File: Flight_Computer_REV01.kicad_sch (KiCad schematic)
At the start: 21 parts, among them CON1 AVR-JTAG-10, J10 Conn_02x12_Odd_Even, J2 Conn_02x03_Counter_Clockwise, J3 Conn_02x03_Counter_Clockwise, J4 Conn_02x05_Top_Bottom, J5 Conn_02x16_Top_Bottom, J6 Conn_02x16_Top_Bottom, J7 Conn_02x10_Odd_Even, J8 Conn_02x16_Top_Bottom, J9 Conn_02x16_Top_Bottom

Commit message: updated layouts, added motor
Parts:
- removed J4: Conn_02x05_Top_Bottom, Connector_PinHeader_2.54mm:PinHeader_2x05_P2.54mm_Vertical, symbol Connector_Generic:Conn_02x05_Top_Bottom
- added J3: AMB POWER, Connector_PinHeader_2.54mm:PinHeader_2x04_P2.54mm_Vertical, symbol Connector_Generic:Conn_02x04_Counter_Clockwise
- added J4: INPUT POWER PASSTHROUGH, Connector_PinHeader_2.54mm:PinHeader_2x03_P2.54mm_Vertical, symbol Connector_Generic:Conn_02x03_Counter_Clockwise
- CON1: now not fitted
- J7: footprint Connector_PinSocket_2.54mm:PinSocket_2x10_P2.54mm_Vertical -> Connector_PinSocket_2.54mm:PinSocket_2x14_P2.54mm_Vertical; symbol Connector_Generic:Conn_02x10_Odd_Even -> Connector_Generic:Conn_02x14_Odd_Even
- J8: renamed from J10; value Conn_02x12_Odd_Even -> Conn_02x18_Odd_Even; footprint Connector_PinHeader_2.54mm:PinHeader_2x12_P2.54mm_Vertical -> Connector_PinSocket_1.27mm:PinSocket_2x26_P1.27mm_Vertical; symbol Connector_Generic:Conn_02x18_Odd_Even -> Connector_Generic:Conn_02x26_Odd_Even
- renumbered C3 to C1, C4 to C2, C5 to C3, C6 to C4, C7 to C5, C8 to C6, C9 to C7, J2 to J1, J9 to J10, J3 to J2, J8 to J9
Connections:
- net GND: now also J7.11 (Pin_11), J7.12 (Pin_12), J7.13 (Pin_13), J7.14 (Pin_14), J7.19 (Pin_19), J7.20 (Pin_20), J7.21 (Pin_21), J7.22 (Pin_22), J8.30 (Pin_30), J3.2 (Pin_2), J3.4 (Pin_4), J3.6 (Pin_6), J3.8 (Pin_8); no longer J7.10 (Pin_10), J7.15 (Pin_15), J7.16 (Pin_16), J7.17 (Pin_17), J7.18 (Pin_18), J7.5 (Pin_5), J7.7 (Pin_7), J7.8 (Pin_8), J8.24 (Pin_24), J8.36 (Pin_36)
- net MTR_SCLK: now also J8.34 (Pin_34); no longer J8.22 (Pin_22)
- net MTR_SDI: now also J8.20 (Pin_20); no longer J8.14 (Pin_14)
- net MTR_SDO: now also J8.9 (Pin_9); no longer J8.3 (Pin_3)
- net MTR_WHA_EN: now also J8.11 (Pin_11); no longer J8.5 (Pin_5)
- net MTR_WHA_HALLA: now also J8.36 (Pin_36); no longer J8.30 (Pin_30)
- net MTR_WHA_HALLB: now also J8.38 (Pin_38); no longer J8.32 (Pin_32)
- net MTR_WHA_HALLC: now also J8.40 (Pin_40); no longer J8.34 (Pin_34)
- net MTR_WHA_INA_H: now also J8.31 (Pin_31); no longer J8.19 (Pin_19)
- net MTR_WHA_INA_L: now also J8.12 (Pin_12); no longer J8.6 (Pin_6)
- net MTR_WHA_INB_H: now also J8.21 (Pin_21); no longer J8.15 (Pin_15)
- net MTR_WHA_INB_L: now also J8.23 (Pin_23); no longer J8.17 (Pin_17)
- net MTR_WHA_INC_H: now also J8.32 (Pin_32); no longer J8.20 (Pin_20)
- net MTR_WHA_INC_L: now also J8.24 (Pin_24); no longer J8.18 (Pin_18)
- net MTR_WHA_SCS: now also J8.7 (Pin_7); no longer J8.1 (Pin_1)
- net MTR_WHB_EN: now also J8.19 (Pin_19); no longer J8.13 (Pin_13)
- net MTR_WHB_HALLA: now also J8.35 (Pin_35); no longer J8.29 (Pin_29)
- net MTR_WHB_HALLB: now also J8.37 (Pin_37); no longer J8.31 (Pin_31)
- net MTR_WHB_HALLC: now also J8.39 (Pin_39); no longer J8.33 (Pin_33)
- net MTR_WHB_INA_H: now also J8.14 (Pin_14); no longer J8.8 (Pin_8)
- net MTR_WHB_INA_L: now also J8.16 (Pin_16); no longer J8.10 (Pin_10)
- net MTR_WHB_INB_H: now also J8.15 (Pin_15); no longer J8.9 (Pin_9)
- net MTR_WHB_INB_L: now also J8.17 (Pin_17); no longer J8.11 (Pin_11)
- net MTR_WHB_INC_H: now also J8.33 (Pin_33); no longer J8.21 (Pin_21)
- net MTR_WHB_INC_L: now also J8.13 (Pin_13); no longer J8.7 (Pin_7)
- net MTR_WHB_SCS: now also J8.18 (Pin_18); no longer J8.12 (Pin_12)
- net MTR_WHB_WAKE: now also J8.8 (Pin_8); no longer J8.2 (Pin_2)
- net N5V: now also J7.2 (Pin_2), J7.4 (Pin_4); no longer J7.20 (Pin_20)
- net P12V: now also J7.10 (Pin_10); no longer J7.6 (Pin_6)
- net P3V3: now also J8.29 (Pin_29); no longer J8.23 (Pin_23), J8.35 (Pin_35)
- net P4V5: now also J7.15 (Pin_15), J7.16 (Pin_16), J7.17 (Pin_17), J7.18 (Pin_18); no longer J7.11 (Pin_11), J7.12 (Pin_12), J7.13 (Pin_13), J7.14 (Pin_14)
- net P5V: now also J7.1 (Pin_1), J7.3 (Pin_3); no longer J7.19 (Pin_19)
- net VAMB: now also J3.1 (Pin_1), J3.3 (Pin_3), J3.5 (Pin_5), J3.7 (Pin_7); no longer J7.1 (Pin_1), J7.2 (Pin_2), J7.3 (Pin_3), J7.4 (Pin_4)
- net _MTR_WHA_nFAULT: now also J8.22 (Pin_22); no longer J8.16 (Pin_16)
- net _MTR_WHB_nFAULT: now also J8.10 (Pin_10); no longer J8.4 (Pin_4)
- new net: J7.5 (Pin_5), J7.7 (Pin_7)
- new net: J7.6 (Pin_6), J7.8 (Pin_8)
- new net 28_IN: J4.1 (Pin_1), J4.2 (Pin_2), J4.3 (Pin_3)
- new net 28_RET: J4.4 (Pin_4), J4.5 (Pin_5), J4.6 (Pin_6)
- new net MTR_WHA_VSNS_A: J8.42 (Pin_42)
- new net MTR_WHA_VSNS_B: J8.44 (Pin_44)
- new net MTR_WHA_VSNS_C: J8.46 (Pin_46)
- new net MTR_WHB_VSNS_A: J8.41 (Pin_41)
- new net MTR_WHB_VSNS_B: J8.43 (Pin_43)
- new net MTR_WHB_VSNS_C: J8.45 (Pin_45)
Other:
- added sheet Motor (Motor.kicad_sch)

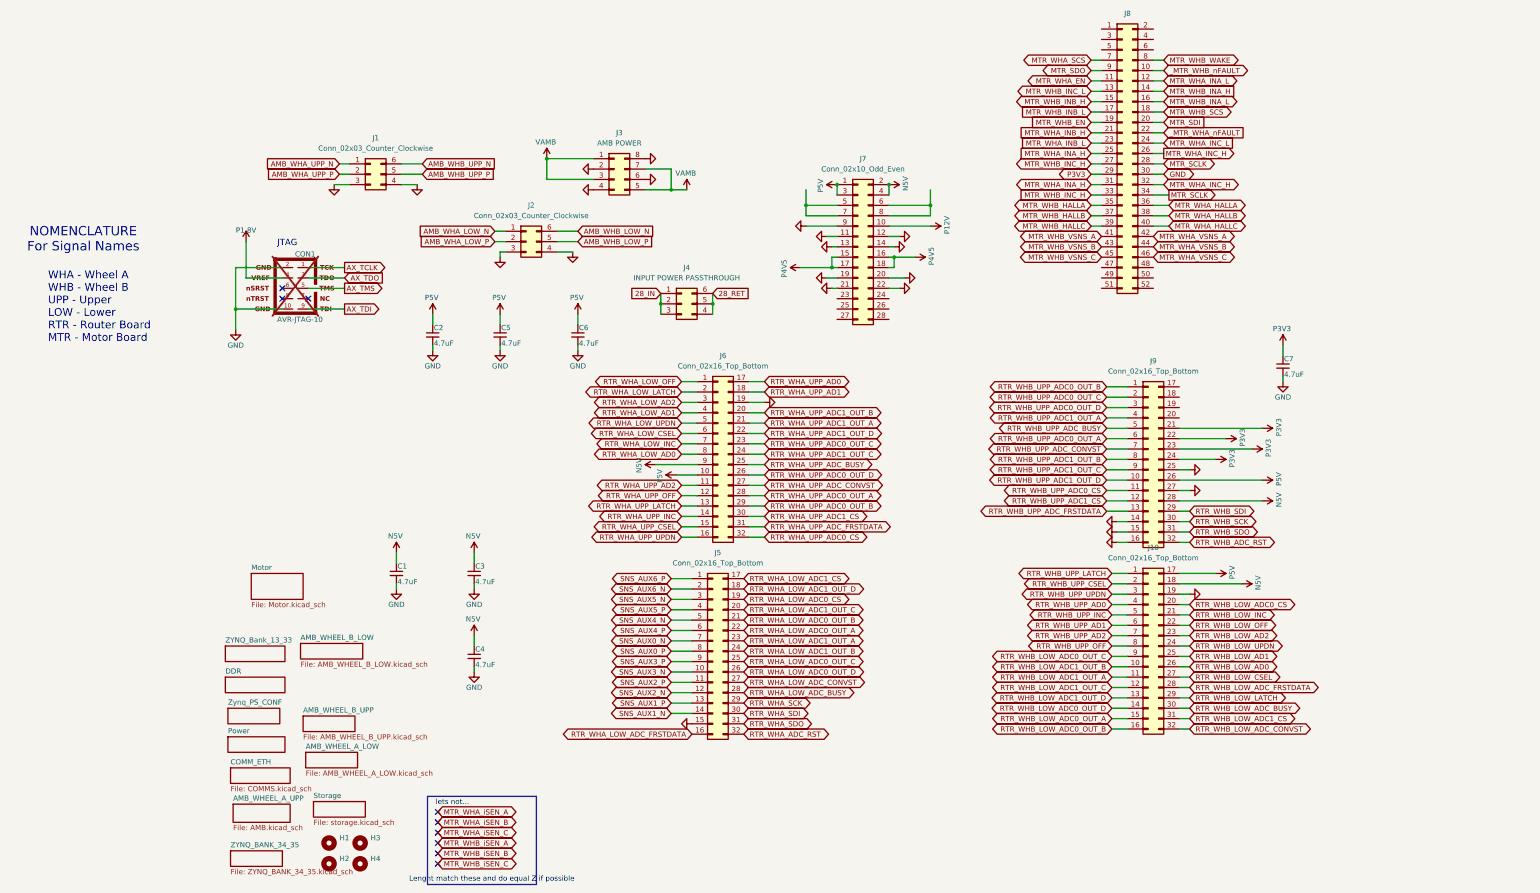
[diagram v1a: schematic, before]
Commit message: Changes to layout pins
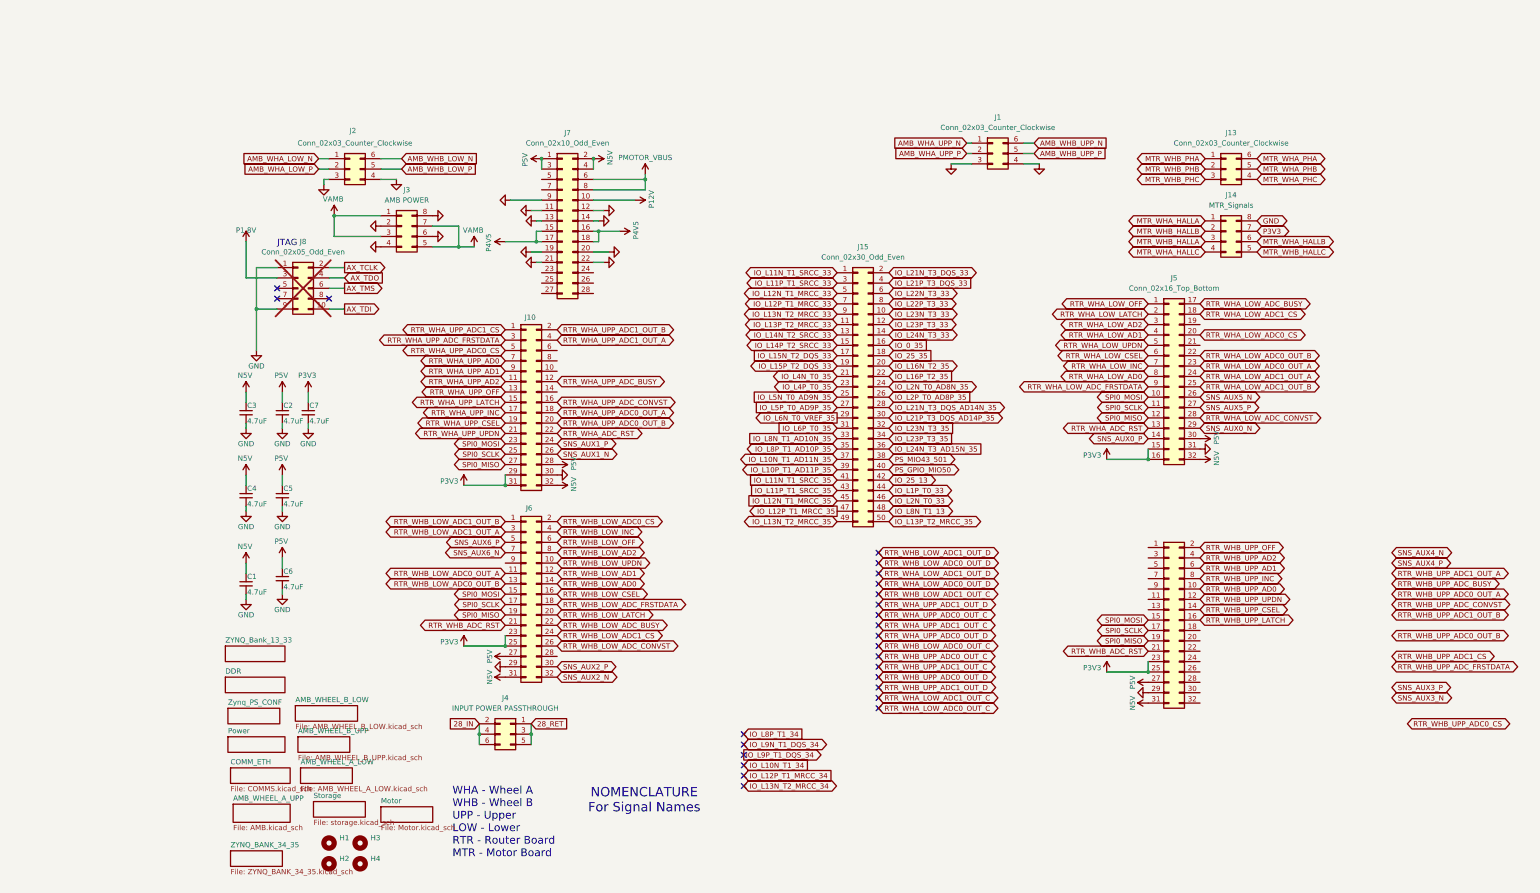
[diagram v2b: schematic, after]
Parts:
- removed CON1: AVR-JTAG-10, Connector_IDC:IDC-Header_2x05_P2.54mm_Vertical, symbol DFTBoard-rescue:AVR-JTAG-10-
- removed J8: Conn_02x18_Odd_Even, Connector_PinSocket_1.27mm:PinSocket_2x26_P1.27mm_Vertical, symbol Connector_Generic:Conn_02x26_Odd_Even
- added J13: Conn_02x03_Counter_Clockwise, Connector_PinHeader_2.54mm:PinHeader_2x03_P2.54mm_Vertical, symbol Connector_Generic:Conn_02x03_Counter_Clockwise
- added J14: MTR_Signals, Connector_PinHeader_1.27mm:PinHeader_2x04_P1.27mm_Vertical, symbol Connector_Generic:Conn_02x04_Counter_Clockwise
- added J15: Conn_02x30_Odd_Even, Connector_PinHeader_1.27mm:PinHeader_2x25_P1.27mm_Vertical, symbol Connector_Generic:Conn_02x25_Odd_Even
- added J8: Conn_02x05_Odd_Even, Connector_PinHeader_2.54mm:PinHeader_2x05_P2.54mm_Vertical, symbol Connector_Generic:Conn_02x05_Odd_Even
- J10, J6, J9: symbol Connector_Generic:Conn_02x16_Top_Bottom -> Connector_Generic:Conn_02x16_Odd_Even
- J4: symbol Connector_Generic:Conn_02x03_Counter_Clockwise -> Connector_Generic:Conn_02x03_Odd_Even
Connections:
- net RTR_WHA_SCK is gone; now on net SNS_AUX0_N: J5.29 (Pin_29)
- net RTR_WHA_SDI is gone; now on net P5V: J5.30 (Pin_30)
- net RTR_WHA_SDO is gone; now on net GND: J5.31 (Pin_31)
- net RTR_WHB_SDI is gone; now on net GND: J9.29 (Pin_29)
- net RTR_WHB_SDO is gone; now on net N5V: J9.31 (Pin_31)
- net 28_IN: now also J4.4 (Pin_4), J4.6 (Pin_6); no longer J4.1 (Pin_1), J4.3 (Pin_3)
- net 28_RET: now also J4.1 (Pin_1), J4.3 (Pin_3); no longer J4.4 (Pin_4), J4.6 (Pin_6)
- net AX_TCLK: now also J8.2 (Pin_2)
- net AX_TDI: now also J8.10 (Pin_10)
- net AX_TDO: now also J8.4 (Pin_4)
- net AX_TMS: now also J8.6 (Pin_6)
- net GND: now also J10.30 (Pin_30), J6.29 (Pin_29), J14.8 (Pin_8), J8.1 (Pin_1), J8.9 (Pin_9); no longer J10.19 (Pin_19), J5.15 (Pin_15), J6.19 (Pin_19), J9.14 (Pin_14), J9.15 (Pin_15), J9.16 (Pin_16), J9.25 (Pin_25), J9.27 (Pin_27)
- net MTR_WHA_HALLA: now also J14.1 (Pin_1)
- net MTR_WHA_HALLB: now also J14.6 (Pin_6)
- net MTR_WHA_HALLC: now also J14.4 (Pin_4)
- net MTR_WHB_HALLA: now also J14.3 (Pin_3)
- net MTR_WHB_HALLB: now also J14.2 (Pin_2)
- net MTR_WHB_HALLC: now also J14.5 (Pin_5)
- net N5V: now also J10.32 (Pin_32), J5.32 (Pin_32), J6.31 (Pin_31); no longer J10.18 (Pin_18), J6.9 (Pin_9), J9.28 (Pin_28)
- net P1.8V: now also J8.3 (Pin_3)
- net P3V3: now also J10.29 (Pin_29), J10.31 (Pin_31), J5.15 (Pin_15), J5.16 (Pin_16), J6.23 (Pin_23), J6.25 (Pin_25), J9.25 (Pin_25), J14.7 (Pin_7); no longer J9.21 (Pin_21), J9.22 (Pin_22), J9.24 (Pin_24)
- net P5V: now also J10.28 (Pin_28), J6.27 (Pin_27), J9.27 (Pin_27); no longer J10.17 (Pin_17), J6.10 (Pin_10), J9.26 (Pin_26)
- net RTR_WHA_ADC_RST: now also J10.22 (Pin_22), J5.13 (Pin_13); no longer J5.32 (Pin_32)
- net RTR_WHA_LOW_AD0: now also J5.8 (Pin_8); no longer J6.8 (Pin_8)
- net RTR_WHA_LOW_AD1: now also J5.4 (Pin_4); no longer J6.4 (Pin_4)
- net RTR_WHA_LOW_AD2: now also J5.3 (Pin_3); no longer J6.3 (Pin_3)
- net RTR_WHA_LOW_ADC0_CS: now also J5.20 (Pin_20); no longer J5.19 (Pin_19)
- net RTR_WHA_LOW_ADC0_OUT_A: now also J5.23 (Pin_23); no longer J5.22 (Pin_22)
- net RTR_WHA_LOW_ADC0_OUT_B: now also J5.22 (Pin_22); no longer J5.21 (Pin_21)
- net RTR_WHA_LOW_ADC0_OUT_C: no longer J5.25 (Pin_25)
- net RTR_WHA_LOW_ADC0_OUT_D: no longer J5.26 (Pin_26)
- net RTR_WHA_LOW_ADC1_CS: now also J5.18 (Pin_18); no longer J5.17 (Pin_17)
- net RTR_WHA_LOW_ADC1_OUT_A: now also J5.24 (Pin_24); no longer J5.23 (Pin_23)
- net RTR_WHA_LOW_ADC1_OUT_B: now also J5.25 (Pin_25); no longer J5.24 (Pin_24)
- net RTR_WHA_LOW_ADC1_OUT_C: no longer J5.20 (Pin_20)
- net RTR_WHA_LOW_ADC1_OUT_D: no longer J5.18 (Pin_18)
- net RTR_WHA_LOW_ADC_BUSY: now also J5.17 (Pin_17); no longer J5.28 (Pin_28)
- net RTR_WHA_LOW_ADC_CONVST: now also J5.28 (Pin_28); no longer J5.27 (Pin_27)
- net RTR_WHA_LOW_ADC_FRSTDATA: now also J5.9 (Pin_9); no longer J5.16 (Pin_16)
- net RTR_WHA_LOW_CSEL: now also J5.6 (Pin_6); no longer J6.6 (Pin_6)
- net RTR_WHA_LOW_INC: now also J5.7 (Pin_7); no longer J6.7 (Pin_7)
- net RTR_WHA_LOW_LATCH: now also J5.2 (Pin_2); no longer J6.2 (Pin_2)
- net RTR_WHA_LOW_OFF: now also J5.1 (Pin_1); no longer J6.1 (Pin_1)
- net RTR_WHA_LOW_UPDN: now also J5.5 (Pin_5); no longer J6.5 (Pin_5)
- net RTR_WHA_UPP_AD0: now also J10.7 (Pin_7); no longer J6.17 (Pin_17)
- net RTR_WHA_UPP_AD1: now also J10.9 (Pin_9); no longer J6.18 (Pin_18)
- net RTR_WHA_UPP_AD2: now also J10.11 (Pin_11); no longer J6.11 (Pin_11)
- net RTR_WHA_UPP_ADC0_CS: now also J10.5 (Pin_5); no longer J6.32 (Pin_32)
- net RTR_WHA_UPP_ADC0_OUT_A: now also J10.18 (Pin_18); no longer J6.28 (Pin_28)
- net RTR_WHA_UPP_ADC0_OUT_B: now also J10.20 (Pin_20); no longer J6.29 (Pin_29)
- net RTR_WHA_UPP_ADC0_OUT_C: no longer J6.23 (Pin_23)
- net RTR_WHA_UPP_ADC0_OUT_D: no longer J6.26 (Pin_26)
- net RTR_WHA_UPP_ADC1_CS: now also J10.1 (Pin_1); no longer J6.30 (Pin_30)
- net RTR_WHA_UPP_ADC1_OUT_A: now also J10.4 (Pin_4); no longer J6.21 (Pin_21)
- net RTR_WHA_UPP_ADC1_OUT_B: now also J10.2 (Pin_2); no longer J6.20 (Pin_20)
- net RTR_WHA_UPP_ADC1_OUT_C: no longer J6.24 (Pin_24)
- net RTR_WHA_UPP_ADC1_OUT_D: no longer J6.22 (Pin_22)
- net RTR_WHA_UPP_ADC_BUSY: now also J10.12 (Pin_12); no longer J6.25 (Pin_25)
- net RTR_WHA_UPP_ADC_CONVST: now also J10.16 (Pin_16); no longer J6.27 (Pin_27)
- net RTR_WHA_UPP_ADC_FRSTDATA: now also J10.3 (Pin_3); no longer J6.31 (Pin_31)
- net RTR_WHA_UPP_CSEL: now also J10.19 (Pin_19); no longer J6.15 (Pin_15)
- net RTR_WHA_UPP_INC: now also J10.17 (Pin_17); no longer J6.14 (Pin_14)
- net RTR_WHA_UPP_LATCH: now also J10.15 (Pin_15); no longer J6.13 (Pin_13)
- net RTR_WHA_UPP_OFF: now also J10.13 (Pin_13); no longer J6.12 (Pin_12)
- net RTR_WHA_UPP_UPDN: now also J10.21 (Pin_21); no longer J6.16 (Pin_16)
- net RTR_WHB_ADC_RST: now also J6.21 (Pin_21), J9.21 (Pin_21); no longer J9.32 (Pin_32)
- net RTR_WHB_LOW_AD0: now also J6.14 (Pin_14); no longer J10.26 (Pin_26)
- net RTR_WHB_LOW_AD1: now also J6.12 (Pin_12); no longer J10.25 (Pin_25)
- net RTR_WHB_LOW_AD2: now also J6.8 (Pin_8); no longer J10.23 (Pin_23)
- net RTR_WHB_LOW_ADC0_CS: now also J6.2 (Pin_2); no longer J10.20 (Pin_20)
- net RTR_WHB_LOW_ADC0_OUT_A: now also J6.11 (Pin_11); no longer J10.15 (Pin_15)
- net RTR_WHB_LOW_ADC0_OUT_B: now also J6.13 (Pin_13); no longer J10.16 (Pin_16)
- net RTR_WHB_LOW_ADC0_OUT_C: no longer J10.9 (Pin_9)
- net RTR_WHB_LOW_ADC0_OUT_D: no longer J10.14 (Pin_14)
- net RTR_WHB_LOW_ADC1_CS: now also J6.24 (Pin_24); no longer J10.31 (Pin_31)
- net RTR_WHB_LOW_ADC1_OUT_A: now also J6.3 (Pin_3); no longer J10.11 (Pin_11)
- net RTR_WHB_LOW_ADC1_OUT_B: now also J6.1 (Pin_1); no longer J10.10 (Pin_10)
- net RTR_WHB_LOW_ADC1_OUT_C: no longer J10.12 (Pin_12)
- net RTR_WHB_LOW_ADC1_OUT_D: no longer J10.13 (Pin_13)
- net RTR_WHB_LOW_ADC_BUSY: now also J6.22 (Pin_22); no longer J10.30 (Pin_30)
- net RTR_WHB_LOW_ADC_CONVST: now also J6.26 (Pin_26); no longer J10.32 (Pin_32)
- net RTR_WHB_LOW_ADC_FRSTDATA: now also J6.18 (Pin_18); no longer J10.28 (Pin_28)
- net RTR_WHB_LOW_CSEL: now also J6.16 (Pin_16); no longer J10.27 (Pin_27)
- net RTR_WHB_LOW_INC: now also J6.4 (Pin_4); no longer J10.21 (Pin_21)
- net RTR_WHB_LOW_LATCH: now also J6.20 (Pin_20); no longer J10.29 (Pin_29)
- net RTR_WHB_LOW_OFF: now also J6.6 (Pin_6); no longer J10.22 (Pin_22)
- net RTR_WHB_LOW_UPDN: now also J6.10 (Pin_10); no longer J10.24 (Pin_24)
- net RTR_WHB_UPP_AD0: now also J9.10 (Pin_10); no longer J10.4 (Pin_4)
- net RTR_WHB_UPP_AD1: now also J9.6 (Pin_6); no longer J10.6 (Pin_6)
- net RTR_WHB_UPP_AD2: now also J9.4 (Pin_4); no longer J10.7 (Pin_7)
- net RTR_WHB_UPP_ADC0_CS: no longer J9.11 (Pin_11)
- net RTR_WHB_UPP_ADC0_OUT_A: no longer J9.6 (Pin_6)
- net RTR_WHB_UPP_ADC0_OUT_B: no longer J9.1 (Pin_1)
- net RTR_WHB_UPP_ADC0_OUT_C: no longer J9.2 (Pin_2)
- net RTR_WHB_UPP_ADC0_OUT_D: no longer J9.3 (Pin_3)
- net RTR_WHB_UPP_ADC1_CS: no longer J9.12 (Pin_12)
- net RTR_WHB_UPP_ADC1_OUT_A: no longer J9.4 (Pin_4)
- net RTR_WHB_UPP_ADC1_OUT_B: no longer J9.8 (Pin_8)
- net RTR_WHB_UPP_ADC1_OUT_C: no longer J9.9 (Pin_9)
- net RTR_WHB_UPP_ADC1_OUT_D: no longer J9.10 (Pin_10)
- net RTR_WHB_UPP_ADC_BUSY: no longer J9.5 (Pin_5)
- net RTR_WHB_UPP_ADC_CONVST: no longer J9.7 (Pin_7)
- net RTR_WHB_UPP_ADC_FRSTDATA: no longer J9.13 (Pin_13)
- net RTR_WHB_UPP_CSEL: now also J9.14 (Pin_14); no longer J10.2 (Pin_2)
- net RTR_WHB_UPP_INC: now also J9.8 (Pin_8); no longer J10.5 (Pin_5)
- net RTR_WHB_UPP_LATCH: now also J9.16 (Pin_16); no longer J10.1 (Pin_1)
- net RTR_WHB_UPP_OFF: now also J9.2 (Pin_2); no longer J10.8 (Pin_8)
- net RTR_WHB_UPP_UPDN: now also J9.12 (Pin_12); no longer J10.3 (Pin_3)
- net SNS_AUX0_N: no longer J5.7 (Pin_7)
- net SNS_AUX0_P: now also J5.14 (Pin_14); no longer J5.8 (Pin_8)
- net SNS_AUX1_N: now also J10.26 (Pin_26); no longer J5.14 (Pin_14)
- net SNS_AUX1_P: now also J10.24 (Pin_24); no longer J5.13 (Pin_13)
- net SNS_AUX2_N: now also J6.32 (Pin_32); no longer J5.12 (Pin_12)
- net SNS_AUX2_P: now also J6.30 (Pin_30); no longer J5.11 (Pin_11)
- net SNS_AUX3_N: no longer J5.10 (Pin_10)
- net SNS_AUX3_P: no longer J5.9 (Pin_9)
- net SNS_AUX4_N: no longer J5.5 (Pin_5)
- net SNS_AUX4_P: no longer J5.6 (Pin_6)
- net SNS_AUX5_N: now also J5.26 (Pin_26); no longer J5.3 (Pin_3)
- net SNS_AUX5_P: now also J5.27 (Pin_27); no longer J5.4 (Pin_4)
- net SNS_AUX6_N: now also J6.7 (Pin_7); no longer J5.2 (Pin_2)
- net SNS_AUX6_P: now also J6.5 (Pin_5); no longer J5.1 (Pin_1)
- net SPI0_SCLK: now reaches J9.17 (Pin_17)
- net SPI0_SCLK: now also J10.25 (Pin_25), J5.11 (Pin_11), J6.17 (Pin_17)
- net SPI0_MISO: now reaches J9.19 (Pin_19)
- net SPI0_MISO: now also J10.27 (Pin_27), J5.12 (Pin_12), J6.19 (Pin_19)
- net at J7.5 (Pin_5): no longer J7.7 (Pin_7)
- net PMOTOR_VBUS: now reaches J7.6 (Pin_6), J7.8 (Pin_8)
- net RTR_WHB_SCK: no longer names the net of J9.30 (Pin_30)
- new net IO_0_35: J15.16 (Pin_16)
- new net IO_25_13: J15.42 (Pin_42)
- new net IO_25_35: J15.18 (Pin_18)
- new net IO_L10N_T1_AD11N_35: J15.37 (Pin_37)
- new net IO_L10P_T1_AD11P_35: J15.39 (Pin_39)
- new net IO_L11N_T1_SRCC_33: J15.1 (Pin_1)
- new net IO_L11N_T1_SRCC_35: J15.41 (Pin_41)
- new net IO_L11P_T1_SRCC_33: J15.3 (Pin_3)
- new net IO_L11P_T1_SRCC_35: J15.43 (Pin_43)
- new net IO_L12N_T1_MRCC_33: J15.5 (Pin_5)
- new net IO_L12N_T1_MRCC_35: J15.45 (Pin_45)
- new net IO_L12P_T1_MRCC_33: J15.7 (Pin_7)
- new net IO_L12P_T1_MRCC_35: J15.47 (Pin_47)
- new net IO_L13N_T2_MRCC_33: J15.9 (Pin_9)
- new net IO_L13N_T2_MRCC_35: J15.49 (Pin_49)
- new net IO_L13P_T2_MRCC_33: J15.11 (Pin_11)
- new net IO_L13P_T2_MRCC_35: J15.50 (Pin_50)
- new net IO_L14N_T2_SRCC_33: J15.13 (Pin_13)
- new net IO_L14P_T2_SRCC_33: J15.15 (Pin_15)
- new net IO_L15N_T2_DQS_33: J15.17 (Pin_17)
- new net IO_L15P_T2_DQS_33: J15.19 (Pin_19)
- new net IO_L16N_T2_35: J15.20 (Pin_20)
- new net IO_L16P_T2_35: J15.22 (Pin_22)
- new net IO_L1P_T0_33: J15.44 (Pin_44)
- new net IO_L21N_T3_DQS_33: J15.2 (Pin_2)
- new net IO_L21N_T3_DQS_AD14N_35: J15.28 (Pin_28)
- new net IO_L21P_T3_DQS_33: J15.4 (Pin_4)
- new net IO_L21P_T3_DQS_AD14P_35: J15.30 (Pin_30)
- new net IO_L22N_T3_33: J15.6 (Pin_6)
- new net IO_L22P_T3_33: J15.8 (Pin_8)
- new net IO_L23N_T3_33: J15.10 (Pin_10)
- new net IO_L23N_T3_35: J15.32 (Pin_32)
- new net IO_L23P_T3_33: J15.12 (Pin_12)
- new net IO_L23P_T3_35: J15.34 (Pin_34)
- new net IO_L24N_T3_33: J15.14 (Pin_14)
- new net IO_L24N_T3_AD15N_35: J15.36 (Pin_36)
- new net IO_L2N_T0_33: J15.46 (Pin_46)
- new net IO_L2N_T0_AD8N_35: J15.24 (Pin_24)
- new net IO_L2P_T0_AD8P_35: J15.26 (Pin_26)
- new net IO_L4N_T0_35: J15.21 (Pin_21)
- new net IO_L4P_T0_35: J15.23 (Pin_23)
- new net IO_L5N_T0_AD9N_35: J15.25 (Pin_25)
- new net IO_L5P_T0_AD9P_35: J15.27 (Pin_27)
- new net IO_L6N_T0_VREF_35: J15.29 (Pin_29)
- new net IO_L6P_T0_35: J15.31 (Pin_31)
- new net IO_L8N_T1_13: J15.48 (Pin_48)
- new net IO_L8N_T1_AD10N_35: J15.33 (Pin_33)
- new net IO_L8P_T1_AD10P_35: J15.35 (Pin_35)
- new net MTR_WHA_PHA: J13.6 (Pin_6)
- new net MTR_WHA_PHB: J13.5 (Pin_5)
- new net MTR_WHA_PHC: J13.4 (Pin_4)
- new net MTR_WHB_PHA: J13.1 (Pin_1)
- new net MTR_WHB_PHB: J13.2 (Pin_2)
- new net MTR_WHB_PHC: J13.3 (Pin_3)
- new net PS_GPIO_MIO50: J15.40 (Pin_40)
- new net PS_MIO43_501: J15.38 (Pin_38)
- new net SPI0_MOSI: J10.23 (Pin_23), J5.10 (Pin_10), J6.15 (Pin_15), J9.15 (Pin_15)
- no-connect marks 9 -> 25
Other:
- note removed: "Lenght match these and do equal Z if possible"
- note removed: "lets not..."
- moved on the sheet: C1, C2, C3, C4, C5, C6, C7, J1, J10, J2, J3, J4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
